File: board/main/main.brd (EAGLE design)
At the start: 160 x 100 mm, 30 parts, among them IC1 78m05, U1 24LC256, U2 6N138M

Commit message: latest board changes
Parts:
- removed U1: 24LC256, SparkFun-IC-Memory:SO08
- added D4, D5, D6, D7, D8, D9: SM5817, adafruit:SOD-123FL
- added FS3: (no value), SRG:JST_B2B-PH_HEADER
- added J1, J2, J3: SN49B12B, SN49B12B:SWITCHCRAFT_SN49B12B
- added R10, R9: 100, SparkFun-Resistors:1206
- R5: value 10K -> 100
- moved R5 120.8 mm to (-69.8, -35.6)
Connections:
- new net N$14: J1.T, R5.1
- new net N$9: J2.T, R9.1
- net FS3: now also FS3.P2
- net GND: now also D5.A, D7.A, D9.A, FS3.P1, J1.S, J2.S, J3.S; no longer U1.1, U1.2, U1.3, U1.4, U1.7
- net JACK1: now also D4.A, D5.C, R5.2
- net JACK2: now also D6.A, D7.C, R9.2
- net JACK3: now also D8.A, D9.C, R10.2
- net N$12: now also J3.T, R10.1; no longer R5.1, U1.8
- net SCL: no longer U1.6
- net SDA: no longer R5.2, U1.5
- net VCC: now also D4.C, D6.C, D8.C, J1.R, J2.R, J3.R

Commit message: schematic updates
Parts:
- removed D8, D9: SM5817, adafruit:SOD-123FL
- removed PWR_LED: (no value), SRG:JST_B2B-PH_HEADER
- removed R7, R8: 220, SparkFun-Resistors:1206
- added ACT: (no value), SparkFun-LED:LED_3MM
- added C5: 0.1uF, resistor:C1206
- added FS3_LED: (no value), SparkFun-Connectors:1X02
- added Z1: PDZVTR5.1B, zener:SODFL4725X105N
- FS1, FS1_LED, FS2, FS2_LED, FS3: device SRG:JST_B2B-PH_HEADER -> SparkFun-Connectors:1X02
- J1, J2, J3: value SN49B12B -> ACJS-MHOM; device SN49B12B:SWITCHCRAFT_SN49B12B -> ACJS-MHOM:ACJS-MHOM
- R10: value 100 -> 1M
- moved J1 90.4 mm to (-55.9, -111.8)
- moved J2 70.1 mm to (-55.9, -128.3)
- moved R10 61.0 mm to (-69.8, -162.6)
- moved J3 57.5 mm to (-55.9, -144.8)
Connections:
- removed net N$12: J3.T, R10.1
- removed net N$4: FS1_LED.P1, R7.1
- removed net N$6: FS2_LED.P1, R8.1
- removed net USB_GND: MICRO.4, USB.GND
- new net N$15: C5.2, PRO_MICRO.17
- net ACT_LED: now also R6.1; no longer PWR_LED.P2
- net FS1: now also FS1.2; no longer FS1.P2
- net FS1_LED: now also FS1_LED.2; no longer FS1_LED.P2
- net FS2: now also FS2.2; no longer FS2.P2
- net FS2_LED: now also FS2_LED.2; no longer FS2_LED.P2
- net FS3: now also FS3.2; no longer FS3.P2
- net FS3_LED: now also FS3_LED.2
- net GND: now also ACT.K, C5.1, FS1.1, FS1_LED.1, FS2.1, FS2_LED.1, FS3.1, FS3_LED.1, J1.TN, J2.TN, J3.TN, R10.1, USB.GND, Z1.2; no longer D9.A, FS1.P1, FS2.P1, FS3.P1, R6.2, R7.2, R8.2
- net JACK3: now also J3.T, Z1.1; no longer D8.A, D9.C
- net N$1: now also ACT.A, R6.2; no longer PWR_LED.P1, R6.1
- net VBUS: no longer MICRO.1
- net VCC: no longer D8.C, J3.R

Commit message: updating components
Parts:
- removed J1, J2, J3: ACJS-MHOM, ACJS-MHOM:ACJS-MHOM
- added EXP1, EXP2, TRIG: ACJS-MHOM, ACJS-MHOM:ACJS-MHOM
- PWR: value DCJ0202 -> PJ-066A; device con-jack:DCJ0202 -> PJ-066A:CUI_PJ-066A
- moved Z1 280.0 mm to (122.0, 38.7)
- moved R10 273.7 mm to (123.2, 31.5), turned to 270 degrees
- moved R9 215.7 mm to (119.2, 31.5), turned to 90 degrees
- moved D6 202.5 mm to (111.2, 29.0), turned to 90 degrees
- moved C5 202.2 mm to (33.1, 17.8)
- moved D7 201.6 mm to (115.3, 29.0), turned to 90 degrees
- moved ACT 195.2 mm to (16.6, 7.17), turned to 180 degrees
- moved D5 180.5 mm to (107.2, 29.0), turned to 90 degrees
- moved D4 175.9 mm to (103.2, 29.0), turned to 90 degrees
- moved R5 172.3 mm to (90.2, 28.4), turned to 180 degrees
- moved FS1 155.9 mm to (112.6, 43.0)
- moved FS1_LED 155.9 mm to (105.0, 43.0)
- moved D1 143.1 mm to (97.1, 34.6), turned to 90 degrees
- moved R4 140.7 mm to (74.6, 39.1)
- moved R3 139.1 mm to (70.7, 22.1)
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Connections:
- net GND: now also EXP1.S, EXP1.TN, EXP2.S, EXP2.TN, TRIG.S, TRIG.TN; no longer J1.S, J1.TN, J2.S, J2.TN, J3.S, J3.TN
- net JACK3: now also TRIG.T; no longer J3.T
- net N$14: now also EXP1.T; no longer J1.T
- net N$9: now also EXP2.T; no longer J2.T
- net VCC: now also EXP1.R, EXP2.R; no longer J1.R, J2.R
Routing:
- net JACK3: track 0.00 -> 128.4 mm, vias 0 -> 2
- net VCC: track 0.00 -> 124.6 mm
- net JACK2: track 0.00 -> 104.6 mm, vias 0 -> 2
- net FS1: track 0.00 -> 98.9 mm, vias 0 -> 1
- net JACK1: track 0.00 -> 87.4 mm, vias 0 -> 2
- net N$10: track 0.00 -> 85.6 mm
- net FS1_LED: track 0.00 -> 85.3 mm
- net N$2: track 0.00 -> 78.8 mm, vias 0 -> 1
- net VIN: track 0.00 -> 78.6 mm, vias 0 -> 2
- net N$13: track 0.00 -> 66.4 mm
- net RESET: track 0.00 -> 59.5 mm
- net FS2: track 0.00 -> 59.0 mm, vias 0 -> 2
- net RAW: track 0.00 -> 56.6 mm, vias 0 -> 1
- net FS2_LED: track 0.00 -> 44.4 mm, vias 0 -> 1
- net RX: track 0.00 -> 40.9 mm
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- added copper zone on layer 1, net GND
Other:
- board size 160 x 100 mm -> 127 x 45 mm
- board text added: "09/07/2020 REV: A"
- board text added: "ZDS Shifter Pro"

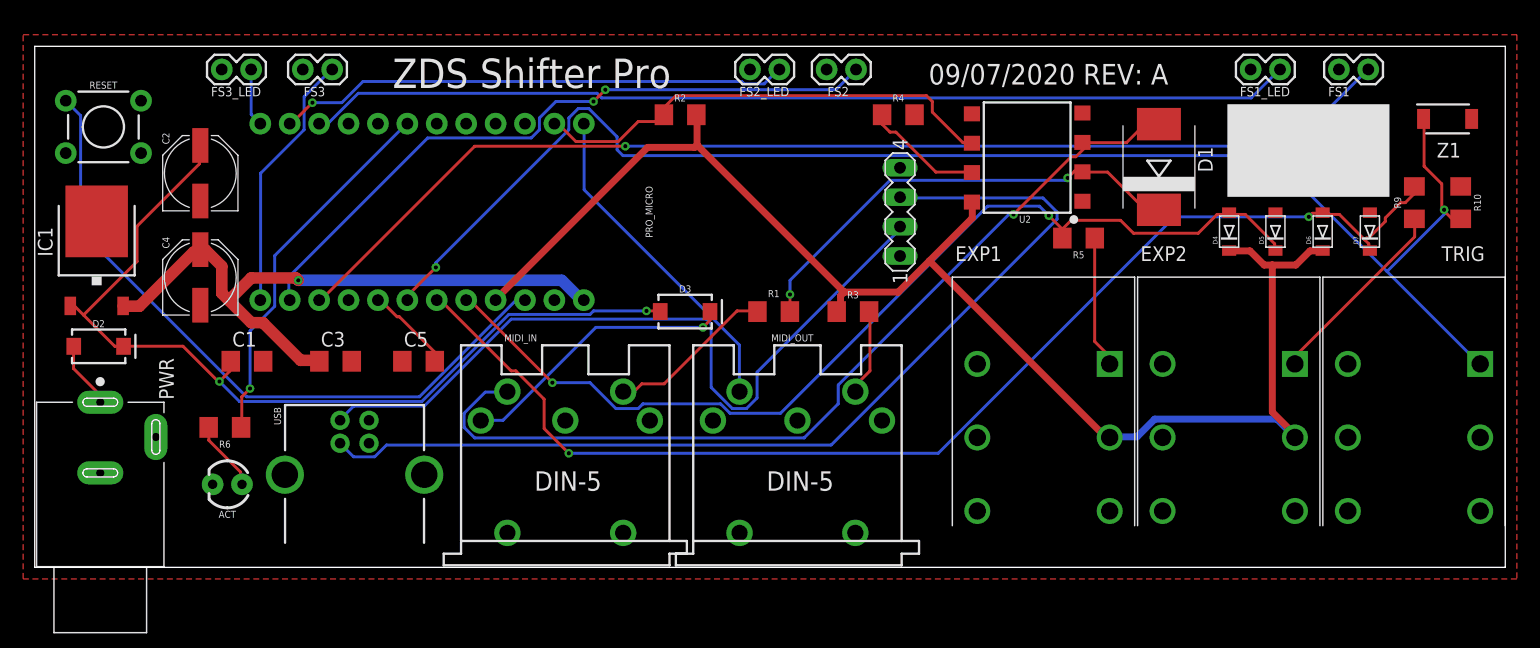
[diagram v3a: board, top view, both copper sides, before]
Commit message: Switch to teensy (#1)
* finalized buttons

* board updates

* 3d print of button template

* code compiles for teensy successfully (still need to test)

* midi is working

* expression pedals are working

* turning on both

placing a 1K resistor between pin 16 and ground

* essentially working

* add todo

* submitting main board to jlcpcb
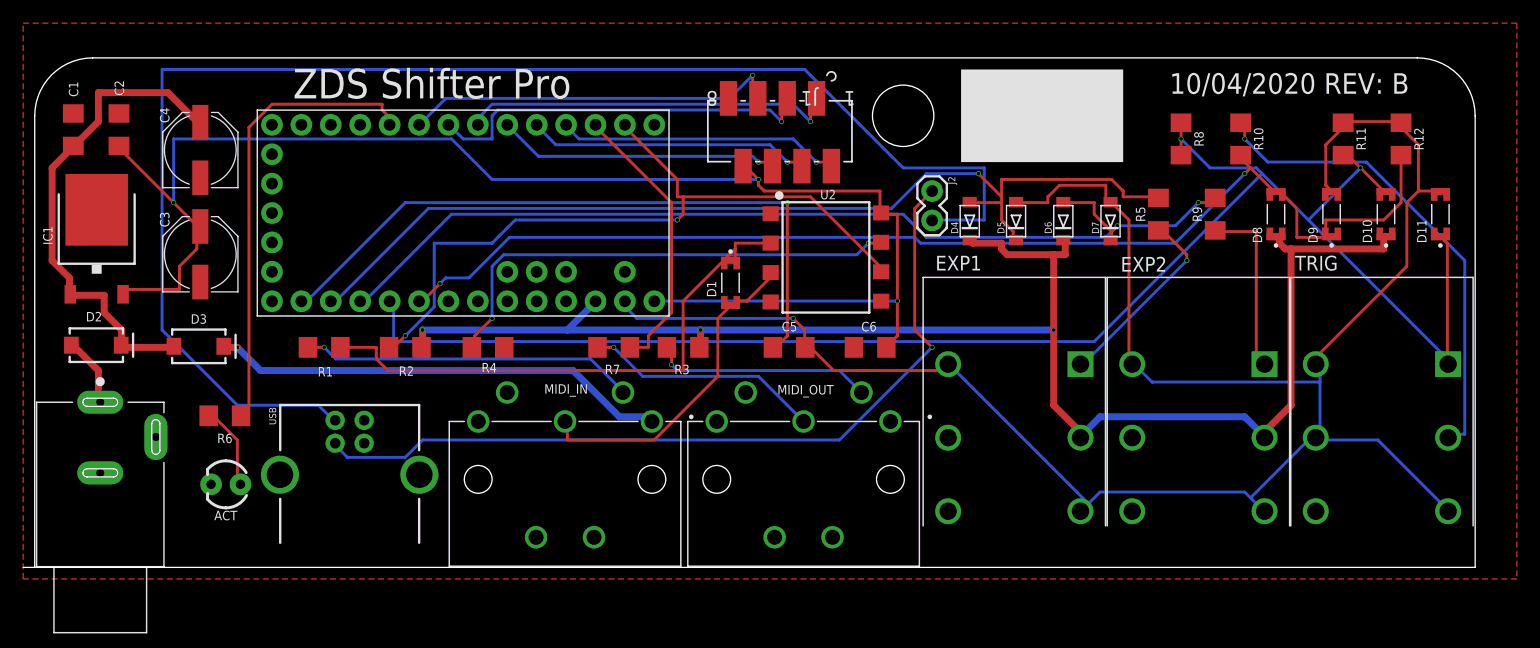
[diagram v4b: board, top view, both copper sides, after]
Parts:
- removed FS1, FS1_LED, FS2, FS2_LED, FS3, FS3_LED: (no value), SparkFun-Connectors:1X02
- removed MICRO: PINS, con-lstb:MA04-1
- removed PRO_MICRO: (no value), SparkFun-Boards:SPARKFUN_PRO_MICRO
- removed RESET: (no value), SparkFun-Switches:TACTILE_SWITCH_PTH_6.0MM
- removed Z1: PDZVTR5.1B, zener:SODFL4725X105N
- added B1: TEENSY-3.1NOSILK, SparkFun-Boards:TEENSY-3.1_NOSILK
- added C6: 0.1uF, resistor:C1206
- added D10, D11, D8, D9: LL4148, LL4148:DIO_LL4148
- added J1: 188275-8, ul_1882758:CONN_188275-8_TYC
- added J2: (no value), SparkFun-Connectors:1X02
- added R11, R12: 2.2K, SparkFun-Resistors:1206
- added R7: 47, SparkFun-Resistors:1206
- added R8: 470, SparkFun-Resistors:1206
- C2: value 10uF -> 0.1uF; device SparkFun-Capacitors:PANASONIC_D -> resistor:C1206
- C3: value 0.1uF -> 10uF; device resistor:C1206 -> SparkFun-Capacitors:PANASONIC_D
- D1: device diode:SMC -> LL4148:DIO_LL4148
- MIDI_IN, MIDI_OUT: value (none) -> SDS-50J; device SparkFun-Connectors:DIN5-RA-PTH -> SDS-50J:CUI_SDS-50J
- R10: value 1M -> 470
- R2: value 220 -> 1K
- R3: value 220 -> 47
- R4: value 4.7K -> 10K
- R5, R9: value 100 -> 1K
- moved D3 42.1 mm to (14.2, 19.1)
- moved R4 40.7 mm to (39.1, 19.0)
- moved R1 38.9 mm to (25.0, 19.0)
- moved D1 38.3 mm to (60.1, 24.6), turned to 270 degrees
- moved C5 32.0 mm to (65.2, 19.0), turned to 180 degrees
- moved R2 31.1 mm to (32.0, 19.0), turned to 180 degrees
- moved C1 25.0 mm to (3.33, 37.8), turned to 90 degrees
- moved D4 22.4 mm to (80.8, 29.9)
- moved D5 22.4 mm to (84.8, 29.9)
- moved D6 22.4 mm to (88.8, 29.9)
- moved D7 22.4 mm to (92.9, 29.9)
- moved R10 19.8 mm to (104.2, 37.0)
- moved U2 19.2 mm to (68.5, 26.6), turned to 270 degrees
- moved R9 17.2 mm to (102.0, 30.5)
- moved R3 15.0 mm to (56.0, 19.0), turned to 180 degrees
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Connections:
- removed net N$15: C5.2, PRO_MICRO.17
- removed net RESET: PRO_MICRO.22, RESET.1
- removed net SCL: PRO_MICRO.6
- removed net SDA: PRO_MICRO.5
- removed net VCC: D4.C, D6.C, EXP1.R, EXP2.R, PRO_MICRO.21, R2.2, R3.1, U2.8
- new net 3.3V: B1.3.3V
- new net 3V: B1.3V, D10.C, D4.C, D6.C, D8.C, EXP1.R, EXP2.R, R2.1, R3.1
- new net AGND: B1.AGND, C5.1, D11.A, D5.A, D7.A, D9.A, EXP1.S, EXP1.TN, EXP2.S, EXP2.TN, R11.1, R12.1, TRIG.RN, TRIG.S, TRIG.TN
- new net JACK4: B1.18, D8.A, D9.C, R10.2, R12.2
- new net N$12: R10.1, TRIG.R
- new net N$4: B1.14, C5.2
- new net N$6: MIDI_OUT.2, R7.2
- new net VBAT: B1.VBAT
- new net VUSB: B1.VUSB
- net ACT_LED: now also B1.8; no longer PRO_MICRO.7
- net FS1: now also B1.2, J1.1; no longer FS1.2, PRO_MICRO.15
- net FS1_LED: now also B1.5, J1.2; no longer FS1_LED.2, PRO_MICRO.10
- net FS2: now also B1.3, J1.3; no longer FS2.2, PRO_MICRO.14
- net FS2_LED: now also B1.6, J1.4; no longer FS2_LED.2, PRO_MICRO.11
- net FS3: now also B1.4, J1.5; no longer FS3.2, PRO_MICRO.13
- net FS3_LED: now also B1.7, J1.6; no longer FS3_LED.2, PRO_MICRO.12
- net GND: now also B1.GND, B1.GND1, C2.2, C3.-, C6.2, J1.8, MIDI_IN.5, MIDI_OUT.3; no longer C2.-, C3.2, C5.1, D5.A, D7.A, EXP1.S, EXP1.TN, EXP2.S, EXP2.TN, FS1.1, FS1_LED.1, FS2.1, FS2_LED.1, FS3.1, FS3_LED.1, MIDI_IN.1, MIDI_OUT.2, PRO_MICRO.23, PRO_MICRO.3, PRO_MICRO.4, R10.1, RESET.3, TRIG.S, TRIG.TN, Z1.2
- net JACK1: now also B1.15; no longer PRO_MICRO.20
- net JACK2: now also B1.16; no longer PRO_MICRO.19
- net JACK3: now also B1.17, D10.A, D11.C, R11.2, R8.1, R8.2; no longer PRO_MICRO.18, R10.2, Z1.1
- net N$10: now also J2.1; no longer MICRO.3
- net N$13: now also J2.2; no longer MICRO.2
- net N$2: now also MIDI_IN.2; no longer MIDI_IN.5
- net N$5: now also MIDI_IN.1; no longer MIDI_IN.3
- net RAW: now also C1.1, D2.C, D3.A, IC1.1; no longer C3.1, IC1.2, PRO_MICRO.24
- net RX: now also B1.0, R2.2; no longer PRO_MICRO.2, R2.1
- net TX: now also B1.1, R7.1; no longer MIDI_OUT.5, PRO_MICRO.1
- net VIN: now also B1.VIN, C2.1, C3.+, C6.1, IC1.2, J1.7, U2.8; no longer C1.1, C2.+, D2.C, D3.A, IC1.1
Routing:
- net AGND: track 0.00 -> 177.2 mm, vias 0 -> 1
- net 3V: track 0.00 -> 134.2 mm, vias 0 -> 3
- net VCC: track 124.6 -> 0.00 mm
- net JACK4: track 0.00 -> 102.8 mm, vias 0 -> 2
- net FS1: track 98.9 -> 24.4 mm
- net RESET: track 59.5 -> 0.00 mm
- net N$4: track 0.00 -> 58.7 mm, vias 0 -> 1
- net N$13: track 66.4 -> 124.2 mm
- net FS1_LED: track 85.3 -> 32.9 mm, vias 0 -> 1
- net N$2: track 78.8 -> 28.8 mm, vias 1 -> 0
- net VIN: track 78.6 -> 128.1 mm, vias 2 -> 3
- net N$12: track 0.00 -> 41.4 mm, vias 0 -> 1
- net FS2: track 59.0 -> 24.4 mm, vias 2 -> 1
- net N$11: track 10.3 -> 42.3 mm, vias 0 -> 2
- net FS3_LED: track 5.00 -> 33.0 mm, vias 0 -> 1
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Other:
- board size 127 x 45 mm -> 125.4 x 44 mm
- board text added: "10/04/2020 REV: B"
- board text removed: "09/07/2020 REV: A"

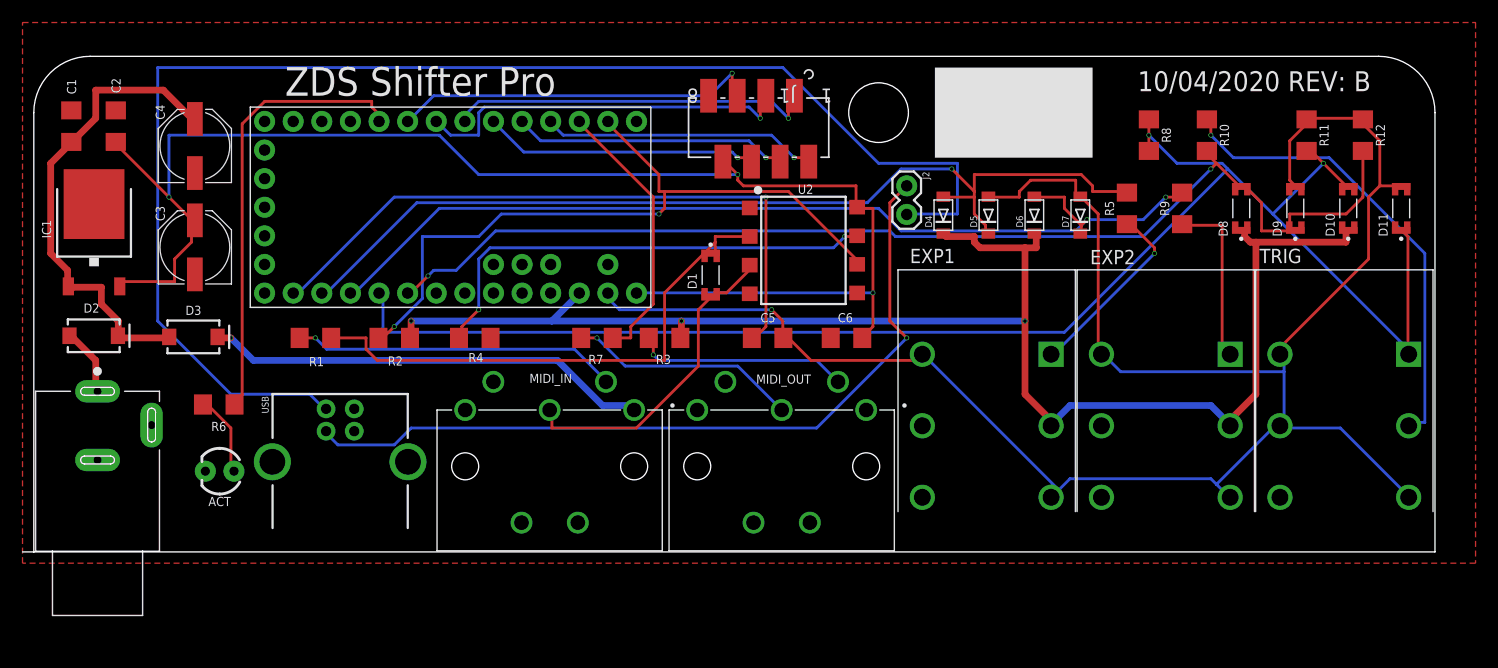
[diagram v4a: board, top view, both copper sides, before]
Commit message: refactoring board
moving to stacked 1/4 jacks to reduce board width
switching to resistor networks and diode arrays to shrink footprint and make assembly a bit easier
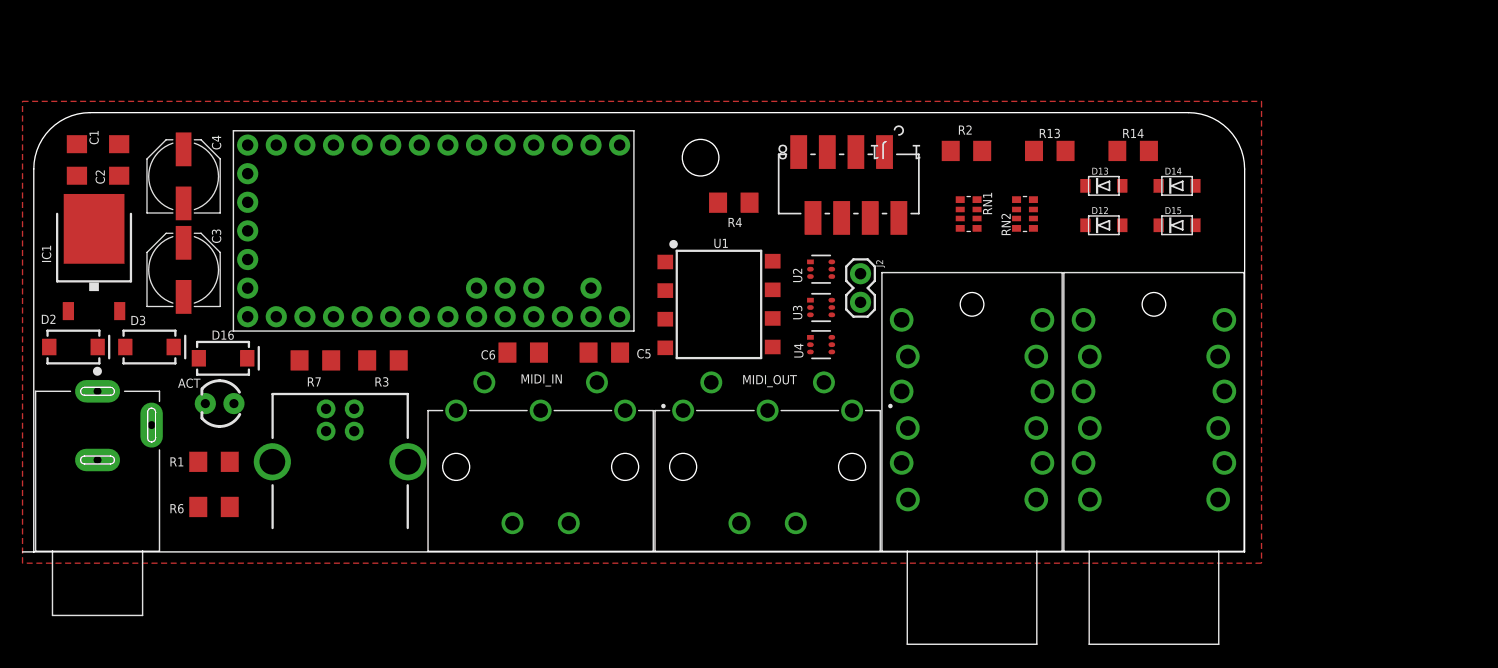
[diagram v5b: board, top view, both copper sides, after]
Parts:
- removed D1: S3M, LL4148:DIO_LL4148
- removed D10, D11, D8, D9: LL4148, LL4148:DIO_LL4148
- removed D4, D5, D6, D7: SM5817, adafruit:SOD-123FL
- removed EXP1, EXP2, TRIG: ACJS-MHOM, ACJS-MHOM:ACJS-MHOM
- removed R10, R8: 470, SparkFun-Resistors:1206
- removed R11, R12: 2.2K, SparkFun-Resistors:1206
- removed R5, R9: 1K, SparkFun-Resistors:1206
- added D12, D13, D14, D15: SM5817, adafruit:SOD-123FL
- added D16: B320AE-13, SparkFun-DiscreteSemi:SMA-DIODE
- added EXP: EXP, ACJS-MHDCM:MHD
- added R13, R14: 1K, SparkFun-Resistors:1206
- added RN1: 470, resistor-dil:EXB38V
- added RN2: 2.2K, resistor-dil:EXB38V
- added TRIG1: TRIG, ACJS-MHDCM:MHD
- added U1: 6N138M, darin-custom:8-SMD
- added U3, U4: MMBD4148TW-7-F, MMBD4148TW7F:SOT-363_DIO
- C1, C2, C6: value 0.1uF -> 0.1uf
- C3, C4: value 10uF -> 10uf
- R6: value 220 -> 130
- U2: value 6N138M -> MMBD4148TW-7-F; device darin-custom:8-SMD -> MMBD4148TW7F:SOT-363_DIO
- moved R2 53.4 mm to (82.8, 35.6)
- moved C6 28.7 mm to (43.5, 17.7)
- moved R4 25.9 mm to (62.1, 31.0)
- moved R3 25.1 mm to (31.0, 17.0)
- moved R7 25.1 mm to (25.0, 17.0)
- moved C5 14.6 mm to (50.6, 17.7)
- moved R1 14.2 mm to (16.0, 8.00)
- moved J1 9.43 mm to (76.8, 35.5)
- moved R6 9.11 mm to (16.0, 3.99)
- moved J2 8.81 mm to (73.4, 24.7)
- moved ACT 6.00 mm to (16.5, 13.2)
- moved D3 4.00 mm to (10.3, 18.2)
- moved C1 3.04 mm to (3.83, 34.8)
- moved C2 3.01 mm to (7.58, 34.8)
- moved C4 2.88 mm to (13.3, 33.3)
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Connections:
- removed net N$14: EXP1.T, R5.1
- removed net N$6 (its old number): MIDI_OUT.2, R7.2
- removed net VBUS: USB.VBUS
- new net JACK5: B1.20, RN1.7, RN2.6, U2.4, U4.1
- new net JACK6: B1.21, RN1.5, RN2.8, U3.6, U4.2
- new net N$15: PWR.3, USB.GND
- new net N$17: D16.A, USB.VBUS
- new net N$18: EXP.12, R13.1
- new net N$21: EXP.6, R14.1
- new net N$8: MIDI_OUT.5, R7.2
- new net SIG-A: MIDI_IN.5, U1.3, U4.3
- new net SIG-C: R1.1, U1.2, U4.4
- net 3V: now also D12.C, D14.C, EXP.11, EXP.5, U3.4, U3.5, U4.5, U4.6; no longer D10.C, D4.C, D6.C, D8.C, EXP1.R, EXP2.R
- net AGND: now also D13.A, D15.A, EXP.10, EXP.3, EXP.4, EXP.9, RN2.1, RN2.2, RN2.3, RN2.4, TRIG1.10, TRIG1.2, TRIG1.3, TRIG1.4, TRIG1.8, TRIG1.9, U2.1, U2.2, U2.3, U3.1; no longer D11.A, D5.A, D7.A, D9.A, EXP1.S, EXP1.TN, EXP2.S, EXP2.TN, R11.1, R12.1, TRIG.RN, TRIG.S, TRIG.TN
- net GND: now also MIDI_IN.1, MIDI_OUT.2, PWR.2, U1.5; no longer MIDI_IN.5, MIDI_OUT.3, PWR.3, U2.5, USB.GND
- net JACK1: now also D12.A, D13.C, R13.2; no longer D4.A, D5.C, R5.2
- net JACK2: now also D14.A, D15.C, R14.2; no longer D6.A, D7.C, R9.2
- net JACK3: now also RN1.6, RN2.7, U2.6, U3.2; no longer D10.A, D11.C, R11.2, R8.1, R8.2, TRIG.T
- net JACK4: now also RN1.8, RN2.5, U2.5, U3.3; no longer D8.A, D9.C, R10.2, R12.2
- net N$11: now also U1.7; no longer U2.7
- net N$12: now also RN1.3, TRIG1.12; no longer R10.1, TRIG.R
- net N$16: now also RN1.1, TRIG1.11; no longer D1.C, R1.1, U2.2
- net N$2: now also RN1.2, TRIG1.6; no longer D1.A, MIDI_IN.2, U2.3
- net N$5: now also MIDI_IN.3; no longer MIDI_IN.1
- net N$9: now also RN1.4, TRIG1.5; no longer EXP2.T, R9.1
- net RX: now also U1.6; no longer U2.6
- net VIN: now also D16.C, U1.8; no longer U2.8
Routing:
- net AGND: track 177.2 -> 0.00 mm, vias 1 -> 0
- net JACK3: track 141.9 -> 0.00 mm, vias 2 -> 0
- net 3V: track 134.2 -> 0.00 mm, vias 3 -> 0
- net VIN: track 128.1 -> 0.00 mm, vias 3 -> 0
- net N$13: track 124.2 -> 0.00 mm
- net JACK4: track 102.8 -> 0.00 mm, vias 2 -> 0
- net JACK2: track 86.4 -> 0.00 mm, vias 2 -> 0
- net JACK1: track 86.4 -> 0.00 mm, vias 1 -> 0
- net N$10: track 70.8 -> 0.00 mm, vias 1 -> 0
- net RX: track 63.4 -> 0.00 mm, vias 2 -> 0
- net N$4: track 58.7 -> 0.00 mm, vias 1 -> 0
- net N$16: track 48.3 -> 0.00 mm
- net N$11: track 42.3 -> 0.00 mm, vias 2 -> 0
- net RAW: track 42.2 -> 0.00 mm
- net N$12: track 41.4 -> 0.00 mm, vias 1 -> 0
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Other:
- board size 125.4 x 44 mm -> 108.5 x 39 mm
- board text added: "?/?/202? REV: C"
- board text added: "EXP"
- board text added: "TRIG"
- board text removed: "10/04/2020 REV: B"
